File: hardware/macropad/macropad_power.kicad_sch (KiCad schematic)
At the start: 27 parts, among them J8 Conn_01x02, Q1 Q_PMOS, Q2 FS8205A, SW12 SW_SPDT, SW13 SW_SPDT, U6 TP4056-42-ESOP8, U7 DW01A, U8 RT8010AGQW, U9 LP2992IM5-3.3/NOPB

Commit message: updated. comments in whatsapp
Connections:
- net VBUS: now also Q1.1 (G); no longer Q1.G
- net out+: now also Q1.2 (S); no longer Q1.S
- net at SW12.2 (B): now also Q1.3 (D); no longer Q1.D
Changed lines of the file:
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@@
 			)
 		)
-		(pin "S"
+		(pin "3"
 		)
-		(pin "G"
+		(pin "2"
 		)
-		(pin "D"
+		(pin "1"
 		)
 		(instances

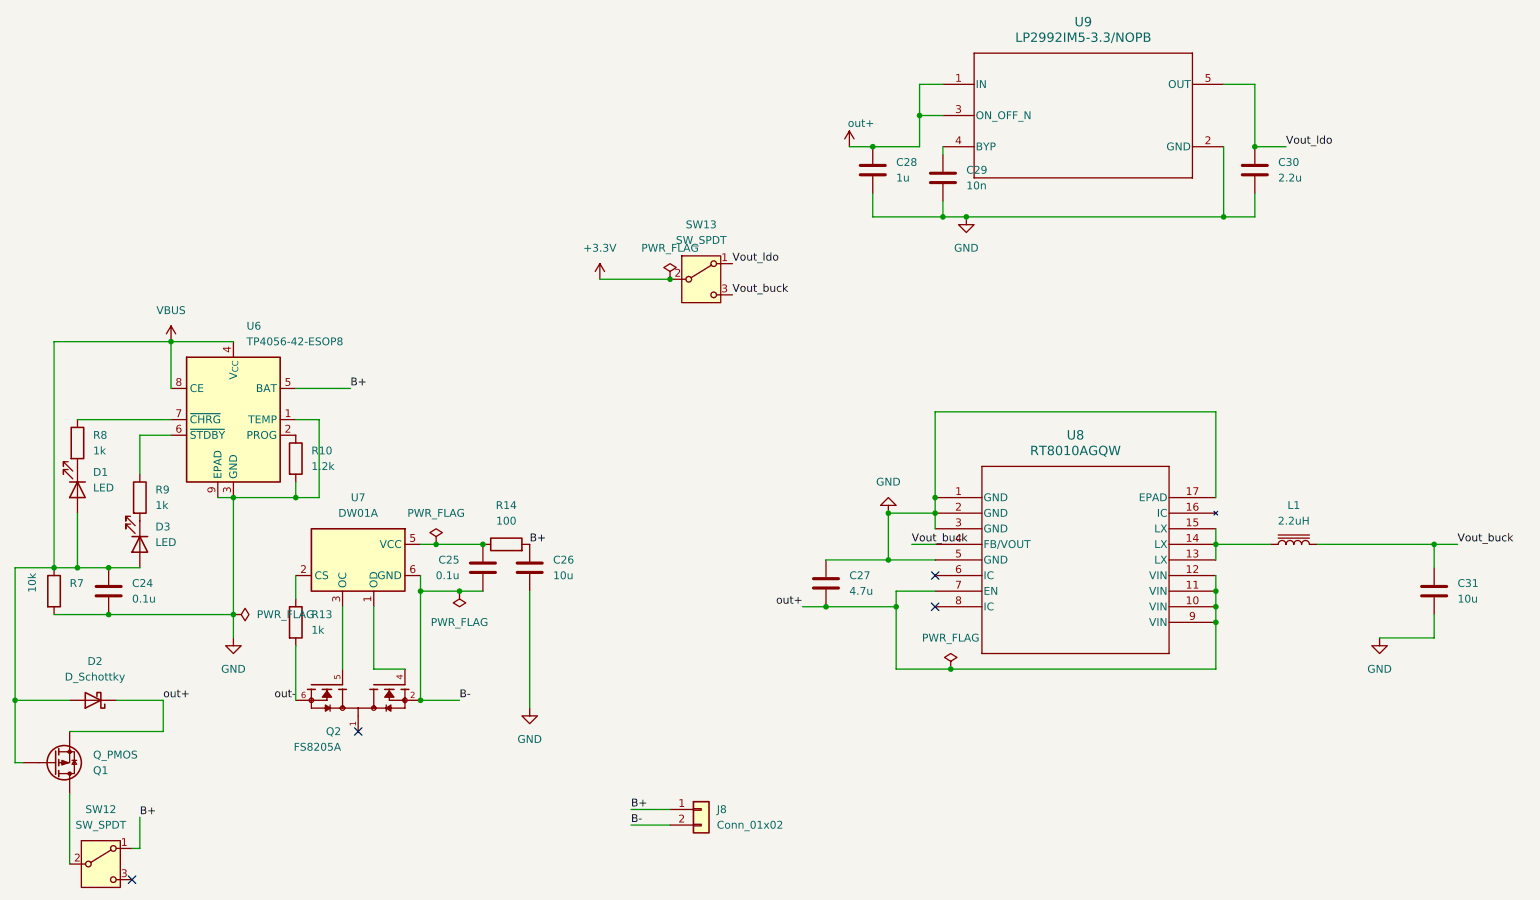
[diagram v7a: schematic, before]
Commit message: updated pcb with switch
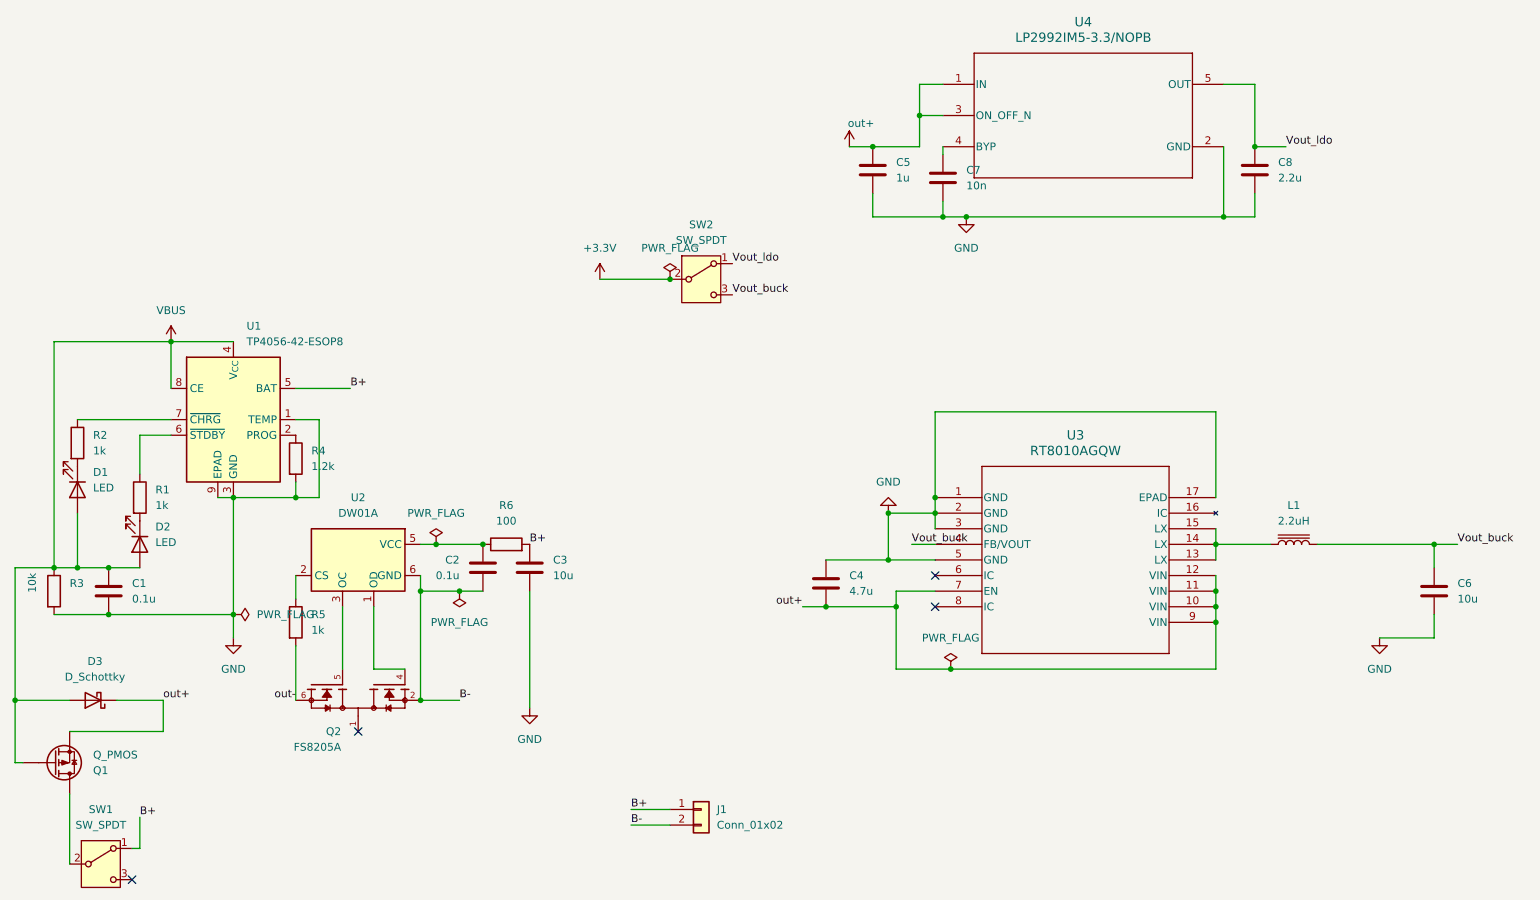
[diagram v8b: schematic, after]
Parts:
- SW1: renamed from SW12; footprint Button_Switch_THT:SW_Slide_SPDT_Angled_CK_OS102011MA1Q -> SS12F23L5:SS12F23L5 spdt
- SW2: renamed from SW13; footprint Button_Switch_THT:SW_Slide_SPDT_Angled_CK_OS102011MA1Q -> SS12F23L5:SS12F23L5 spdt
- renumbered C24 to C1, C25 to C2, C26 to C3, C27 to C4, C28 to C5, C31 to C6, C29 to C7, C30 to C8, D3 to D2, D2 to D3, J8 to J1, R9 to R1, R8 to R2, R7 to R3, R10 to R4, R13 to R5, R14 to R6, U6 to U1, U7 to U2, U8 to U3, U9 to U4
